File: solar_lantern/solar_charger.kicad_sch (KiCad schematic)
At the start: 21 parts, among them Q1 RU20P7C, Q2 RU20P7C, U1 CN3791

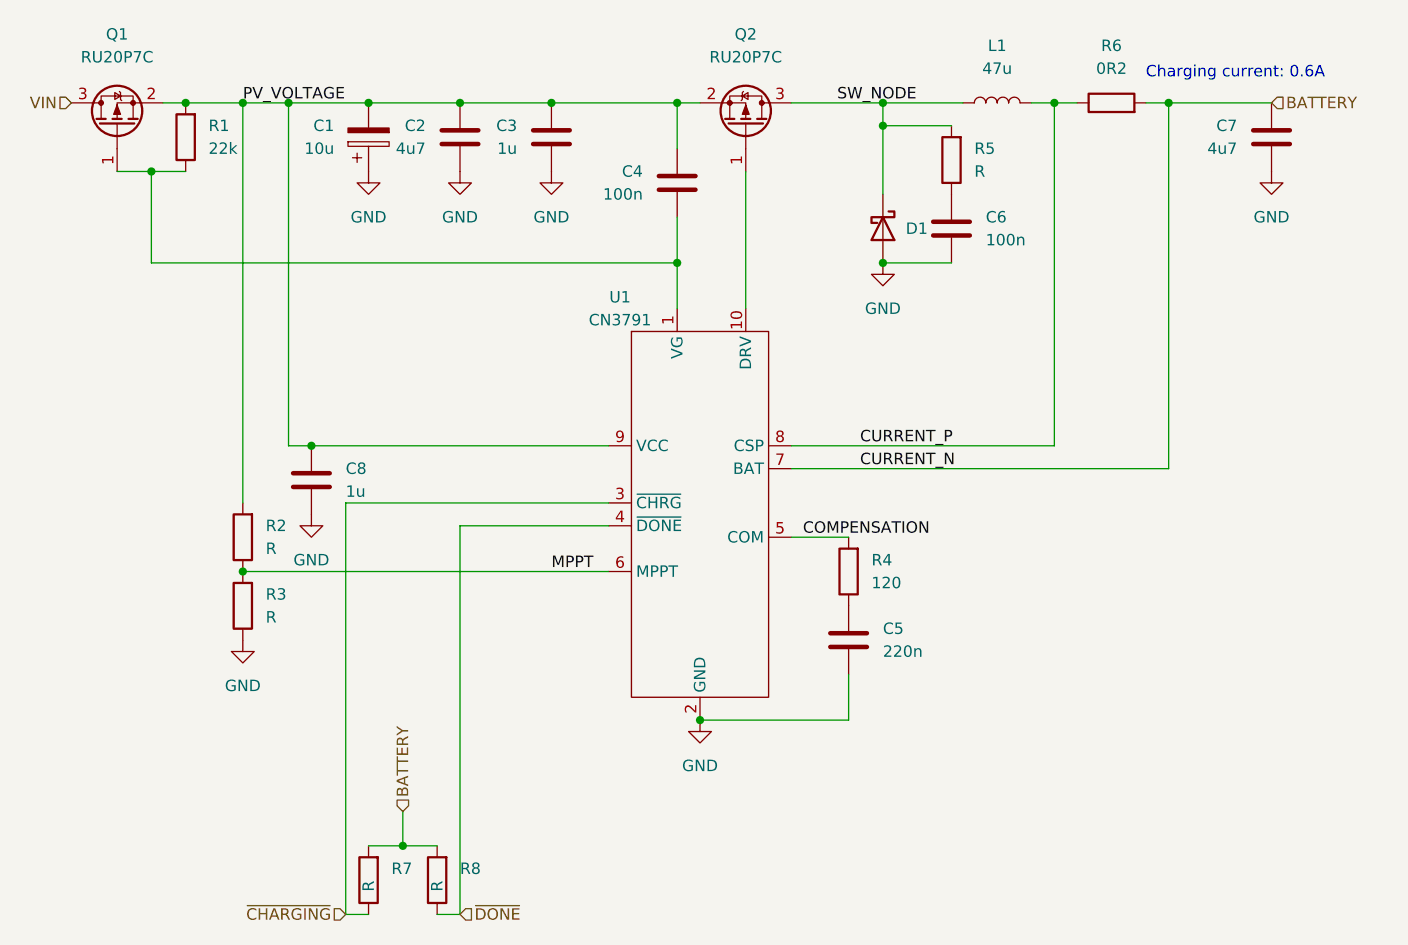
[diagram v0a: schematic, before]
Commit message: Make board smaller, Fix bad cap orientation, Add a diode to reduce quescient current
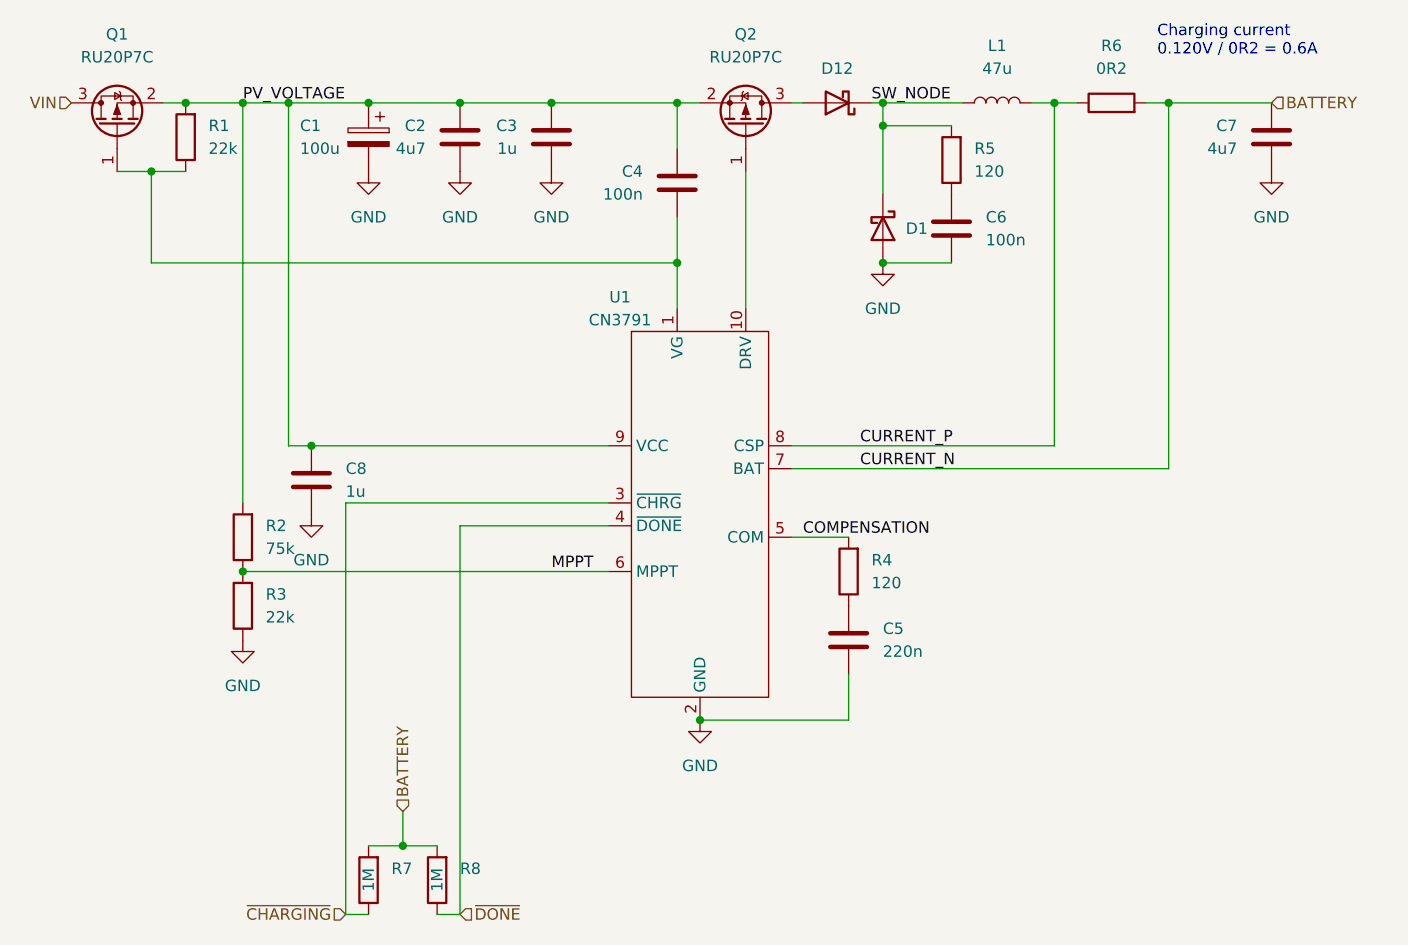
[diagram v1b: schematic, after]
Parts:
- added D12: D_Schottky, Diode_SMD:D_SOD-323, symbol Device:D_Schottky
- C1: value 10u -> 100u; Manufacturer (none) -> KEMET; PartNo (none) -> EEV107M016S9GAA
- R2: value R -> 75k
- R3: value R -> 22k
- R5: value R -> 120
- R7, R8: value R -> 1M
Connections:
- net GND: now also C1.2; no longer C1.1
- net PV_VOLTAGE: now also C1.1; no longer C1.2
- net SW_NODE: now also D12.1 (K); no longer Q2.3 (D)
- new net: D12.2 (A), Q2.3 (D)
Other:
- note added: "Charging current 0.120V / 0R2 = 0.6A"
- note removed: "Charging current: 0.6A"

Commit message: Nicen schematics a bit
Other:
- company: (none) -> Catnip electronics
- title: (none) -> Solar MPPT charger
- moved on the sheet: L1

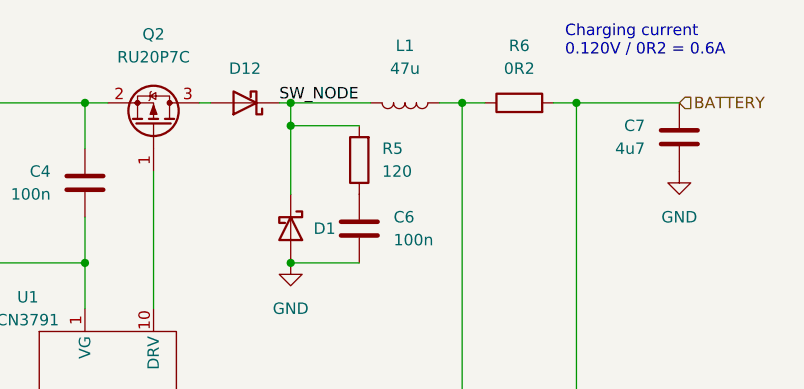
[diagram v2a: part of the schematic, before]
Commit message: Add CERN-OHL_S licence
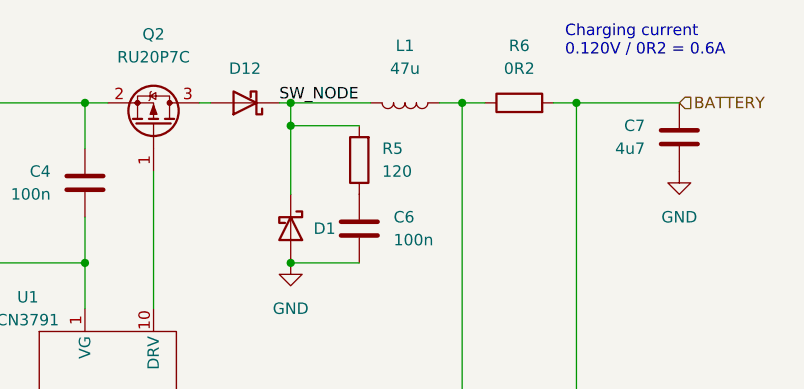
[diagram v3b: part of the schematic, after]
